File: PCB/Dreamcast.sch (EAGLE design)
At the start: 17 parts

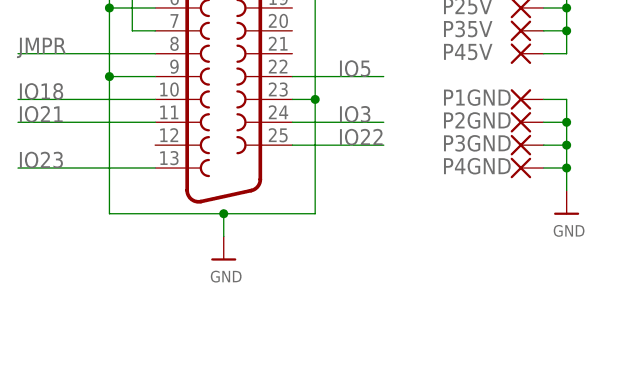
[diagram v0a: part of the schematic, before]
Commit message: Added exposed GND plane at DB25 anchors
All PCBs have been update to have exposed GND plane pads for the DB25 anchor points.

This resolves Issue 54
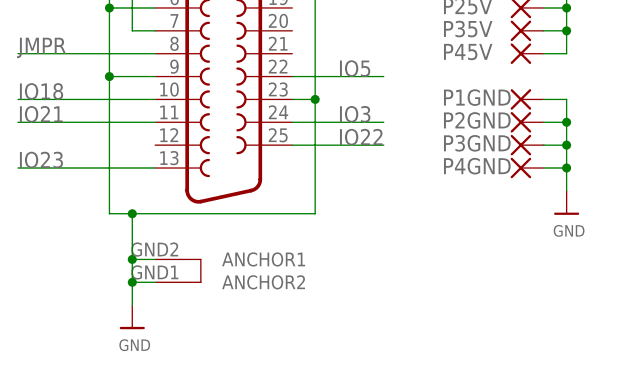
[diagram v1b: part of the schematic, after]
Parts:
- X1: device SparkFun-Retired:DB25_FEMALEH -> SparkFun-Retired:DB25_FEMALEHP
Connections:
- net GND: now also X1.ANCHOR1, X1.ANCHOR2
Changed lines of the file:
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@@
 </classes>
 <parts>
-<part name="X1" library="SparkFun-Retired" deviceset="DB25_FEMALE" device="H"/>
+<part name="X1" library="SparkFun-Retired" deviceset="DB25_FEMALE" device="HP"/>
 <part name="U$53" library="microbuilder" deviceset="VIN" device="" value="5VIN"/>
 <part name="U$54" library="Airquality_Sensor" library_urn="urn:adsk.eagle:library:16015176" deviceset="GND" device=""/>
@@
 <attribute name="VALUE" x="402.336" y="11.176" size="1.27" layer="96"/>
 </instance>
-<instance part="U$54" gate="G$1" x="414.02" y="-38.1" smashed="yes">
-<attribute name="VALUE" x="412.496" y="-40.64" size="1.27" layer="96"/>
+<instance part="U$54" gate="G$1" x="403.86" y="-45.72" smashed="yes">
+<attribute name="VALUE" x="402.336" y="-48.26" size="1.27" layer="96"/>
 </instance>
 <instance part="P3D0" gate="1" x="447.04" y="2.54" smashed="yes">
@@
 <net name="GND" class="0">
 <segment>
-<pinref part="U$54" gate="G$1" pin="GND"/>
-<wire x1="424.18" y1="-33.02" x2="414.02" y2="-33.02" width="0.1524" layer="91"/>
-<wire x1="414.02" y1="-33.02" x2="414.02" y2="-35.56" width="0.1524" layer="91"/>
-<junction x="414.02" y="-33.02"/>
-<wire x1="414.02" y1="-33.02" x2="401.32" y2="-33.02" width="0.1524" layer="91"/>
+<pinref part="P1GND" gate="1" pin="P"/>
+<wire x1="449.58" y1="-20.32" x2="452.12" y2="-20.32" width="0.1524" layer="91"/>
+<pinref part="P4GND" gate="1" pin="P"/>
+<wire x1="449.58" y1="-27.94" x2="452.12" y2="-27.94" width="0.1524" layer="91"/>
+<pinref part="P3GND" gate="1" pin="P"/>
+<wire x1="449.58" y1="-25.4" x2="452.12" y2="-25.4" width="0.1524" layer="91"/>
+<pinref part="P2GND" gate="1" pin="P"/>
+<wire x1="449.58" y1="-22.86" x2="452.12" y2="-22.86" width="0.1524" layer="91"/>
+<pinref part="U$52" gate="G$1" pin="GND"/>
+<wire x1="452.12" y1="-20.32" x2="452.12" y2="-22.86" width="0.1524" layer="91"/>
+<junction x="452.12" y="-22.86"/>
+<wire x1="452.12" y1="-22.86" x2="452.12" y2="-25.4" width="0.1524" layer="91"/>
+<junction x="452.12" y="-25.4"/>
+<wire x1="452.12" y1="-25.4" x2="452.12" y2="-27.94" width="0.1524" layer="91"/>
+<junction x="452.12" y="-27.94"/>
+<wire x1="452.12" y1="-27.94" x2="452.12" y2="-30.48" width="0.1524" layer="91"/>
+</segment>
+<segment>
+<wire x1="424.18" y1="-33.02" x2="403.86" y2="-33.02" width="0.1524" layer="91"/>
 <pinref part="X1" gate="-1" pin="2"/>
+<wire x1="403.86" y1="-33.02" x2="401.32" y2="-33.02" width="0.1524" layer="91"/>
 <wire x1="406.4" y1="0" x2="401.32" y2="0" width="0.1524" layer="91"/>
 <wire x1="401.32" y1="0" x2="401.32" y2="-2.54" width="0.1524" layer="91"/>
@@
 <wire x1="421.64" y1="-20.32" x2="424.18" y2="-20.32" width="0.1524" layer="91"/>
 <junction x="424.18" y="-20.32"/>
-</segment>
-<segment>
-<pinref part="P1GND" gate="1" pin="P"/>
-<wire x1="449.58" y1="-20.32" x2="452.12" y2="-20.32" width="0.1524" layer="91"/>
-<pinref part="P4GND" gate="1" pin="P"/>
-<wire x1="449.58" y1="-27.94" x2="452.12" y2="-27.94" width="0.1524" layer="91"/>
-<pinref part="P3GND" gate="1" pin="P"/>
-<wire x1="449.58" y1="-25.4" x2="452.12" y2="-25.4" width="0.1524" layer="91"/>
-<pinref part="P2GND" gate="1" pin="P"/>
-<wire x1="449.58" y1="-22.86" x2="452.12" y2="-22.86" width="0.1524" layer="91"/>
-<pinref part="U$52" gate="G$1" pin="GND"/>
-<wire x1="452.12" y1="-20.32" x2="452.12" y2="-22.86" width="0.1524" layer="91"/>
-<junction x="452.12" y="-22.86"/>
-<wire x1="452.12" y1="-22.86" x2="452.12" y2="-25.4" width="0.1524" layer="91"/>
-<junction x="452.12" y="-25.4"/>
-<wire x1="452.12" y1="-25.4" x2="452.12" y2="-27.94" width="0.1524" layer="91"/>
-<junction x="452.12" y="-27.94"/>
-<wire x1="452.12" y1="-27.94" x2="452.12" y2="-30.48" width="0.1524" layer="91"/>
+<pinref part="U$54" gate="G$1" pin="GND"/>
+<wire x1="403.86" y1="-33.02" x2="403.86" y2="-38.1" width="0.1524" layer="91"/>
+<junction x="403.86" y="-33.02"/>
+<pinref part="X1" gate="-1" pin="ANCHOR2"/>
+<wire x1="403.86" y1="-38.1" x2="403.86" y2="-40.64" width="0.1524" layer="91"/>
+<wire x1="403.86" y1="-40.64" x2="403.86" y2="-43.18" width="0.1524" layer="91"/>
+<wire x1="406.4" y1="-40.64" x2="403.86" y2="-40.64" width="0.1524" layer="91"/>
+<junction x="403.86" y="-40.64"/>
+<pinref part="X1" gate="-1" pin="ANCHOR1"/>
+<wire x1="406.4" y1="-38.1" x2="403.86" y2="-38.1" width="0.1524" layer="91"/>
+<junction x="403.86" y="-38.1"/>
 </segment>
 </net>
